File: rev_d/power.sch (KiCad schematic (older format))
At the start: 15 parts, among them J1 POWER_SELECT, Q1 PN2222, U1 LTV-826, U2 LTV-826, U3 LTV-826, U4 LTV-826, U5 LM2940, U6 754410

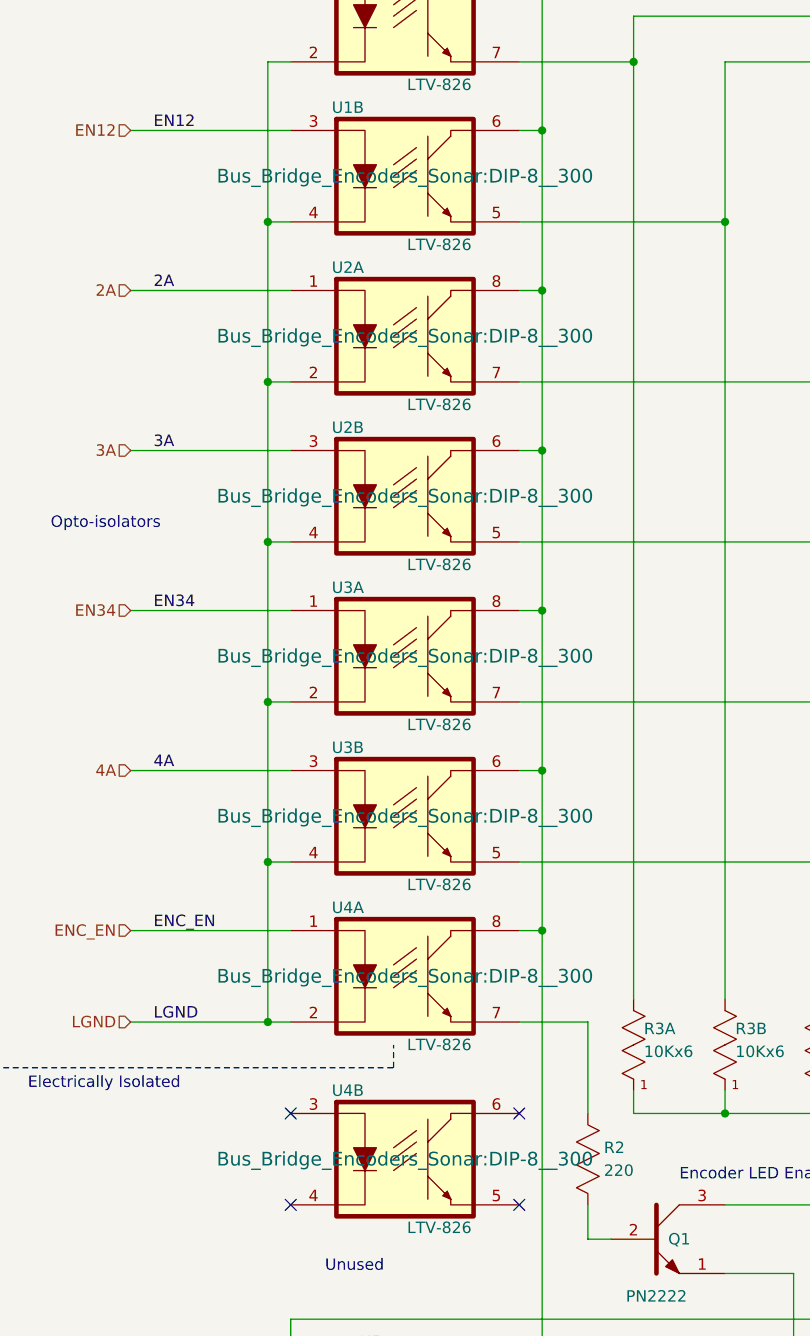
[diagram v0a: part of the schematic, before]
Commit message: Removed some ugliness from schematic.
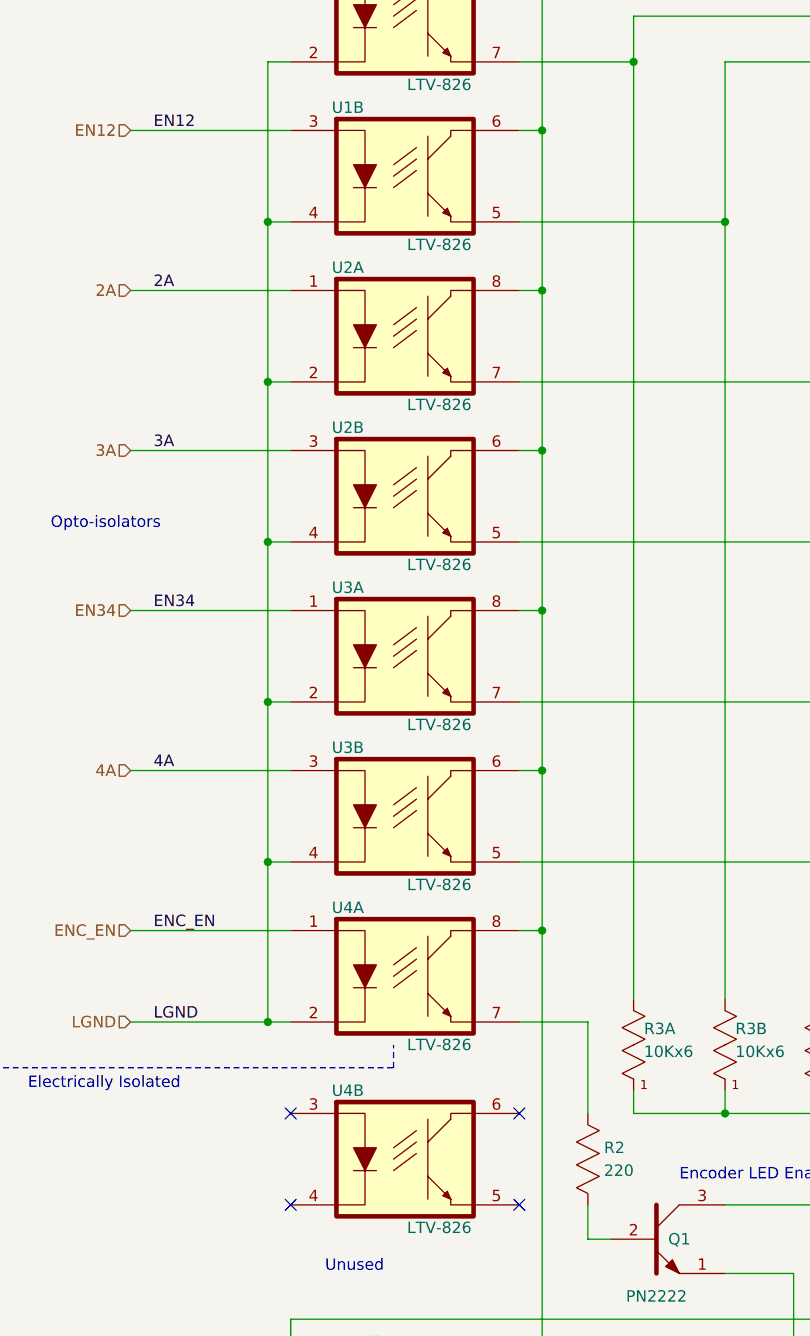
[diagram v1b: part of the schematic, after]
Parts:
- U1: footprint Bus_Bridge_Encoders_Sonar:DIP-8__300 -> (none)
- U2, U3, U4: footprint Bus_Bridge_Encoders_Sonar:DIP-8__300 -> ~
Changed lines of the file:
@@
 F 0 "U1" H 2050 1900 50  0000 C CNN
 F 1 "LTV-826" H 2450 1300 50  0000 C CNN
-F 2 "Bus_Bridge_Encoders_Sonar:DIP-8__300" H 2300 1600 60  0000 C CNN
+F 2 "" H 2300 1600 60  0000 C CNN
 F 3 "" H 2300 1600 60  0000 C CNN
 	2    2300 1600
@@
 F 0 "U2" H 2050 2600 50  0000 C CNN
 F 1 "LTV-826" H 2450 2000 50  0000 C CNN
-F 2 "Bus_Bridge_Encoders_Sonar:DIP-8__300" H 2300 2300 60  0000 C CNN
+F 2 "~" H 2300 2300 60  0000 C CNN
 F 3 "" H 2300 2300 60  0000 C CNN
 	1    2300 2300
@@
 F 0 "U2" H 2050 3300 50  0000 C CNN
 F 1 "LTV-826" H 2450 2700 50  0000 C CNN
-F 2 "Bus_Bridge_Encoders_Sonar:DIP-8__300" H 2300 3000 60  0000 C CNN
+F 2 "~" H 2300 3000 60  0000 C CNN
 F 3 "" H 2300 3000 60  0000 C CNN
 	2    2300 3000
@@
 F 0 "U3" H 2050 4000 50  0000 C CNN
 F 1 "LTV-826" H 2450 3400 50  0000 C CNN
-F 2 "Bus_Bridge_Encoders_Sonar:DIP-8__300" H 2300 3700 60  0000 C CNN
+F 2 "~" H 2300 3700 60  0000 C CNN
 F 3 "" H 2300 3700 60  0000 C CNN
 	1    2300 3700
@@
 F 0 "U3" H 2050 4700 50  0000 C CNN
 F 1 "LTV-826" H 2450 4100 50  0000 C CNN
-F 2 "Bus_Bridge_Encoders_Sonar:DIP-8__300" H 2300 4400 60  0000 C CNN
+F 2 "~" H 2300 4400 60  0000 C CNN
 F 3 "" H 2300 4400 60  0000 C CNN
 	2    2300 4400
@@
 F 0 "U4" H 2050 5400 50  0000 C CNN
 F 1 "LTV-826" H 2450 4800 50  0000 C CNN
-F 2 "Bus_Bridge_Encoders_Sonar:DIP-8__300" H 2300 5100 60  0000 C CNN
+F 2 "~" H 2300 5100 60  0000 C CNN
 F 3 "" H 2300 5100 60  0000 C CNN
 	1    2300 5100
@@
 F 0 "U4" H 2050 6200 50  0000 C CNN
 F 1 "LTV-826" H 2450 5600 50  0000 C CNN
-F 2 "Bus_Bridge_Encoders_Sonar:DIP-8__300" H 2300 5900 60  0000 C CNN
+F 2 "~" H 2300 5900 60  0000 C CNN
 F 3 "" H 2300 5900 60  0000 C CNN
 	2    2300 5900

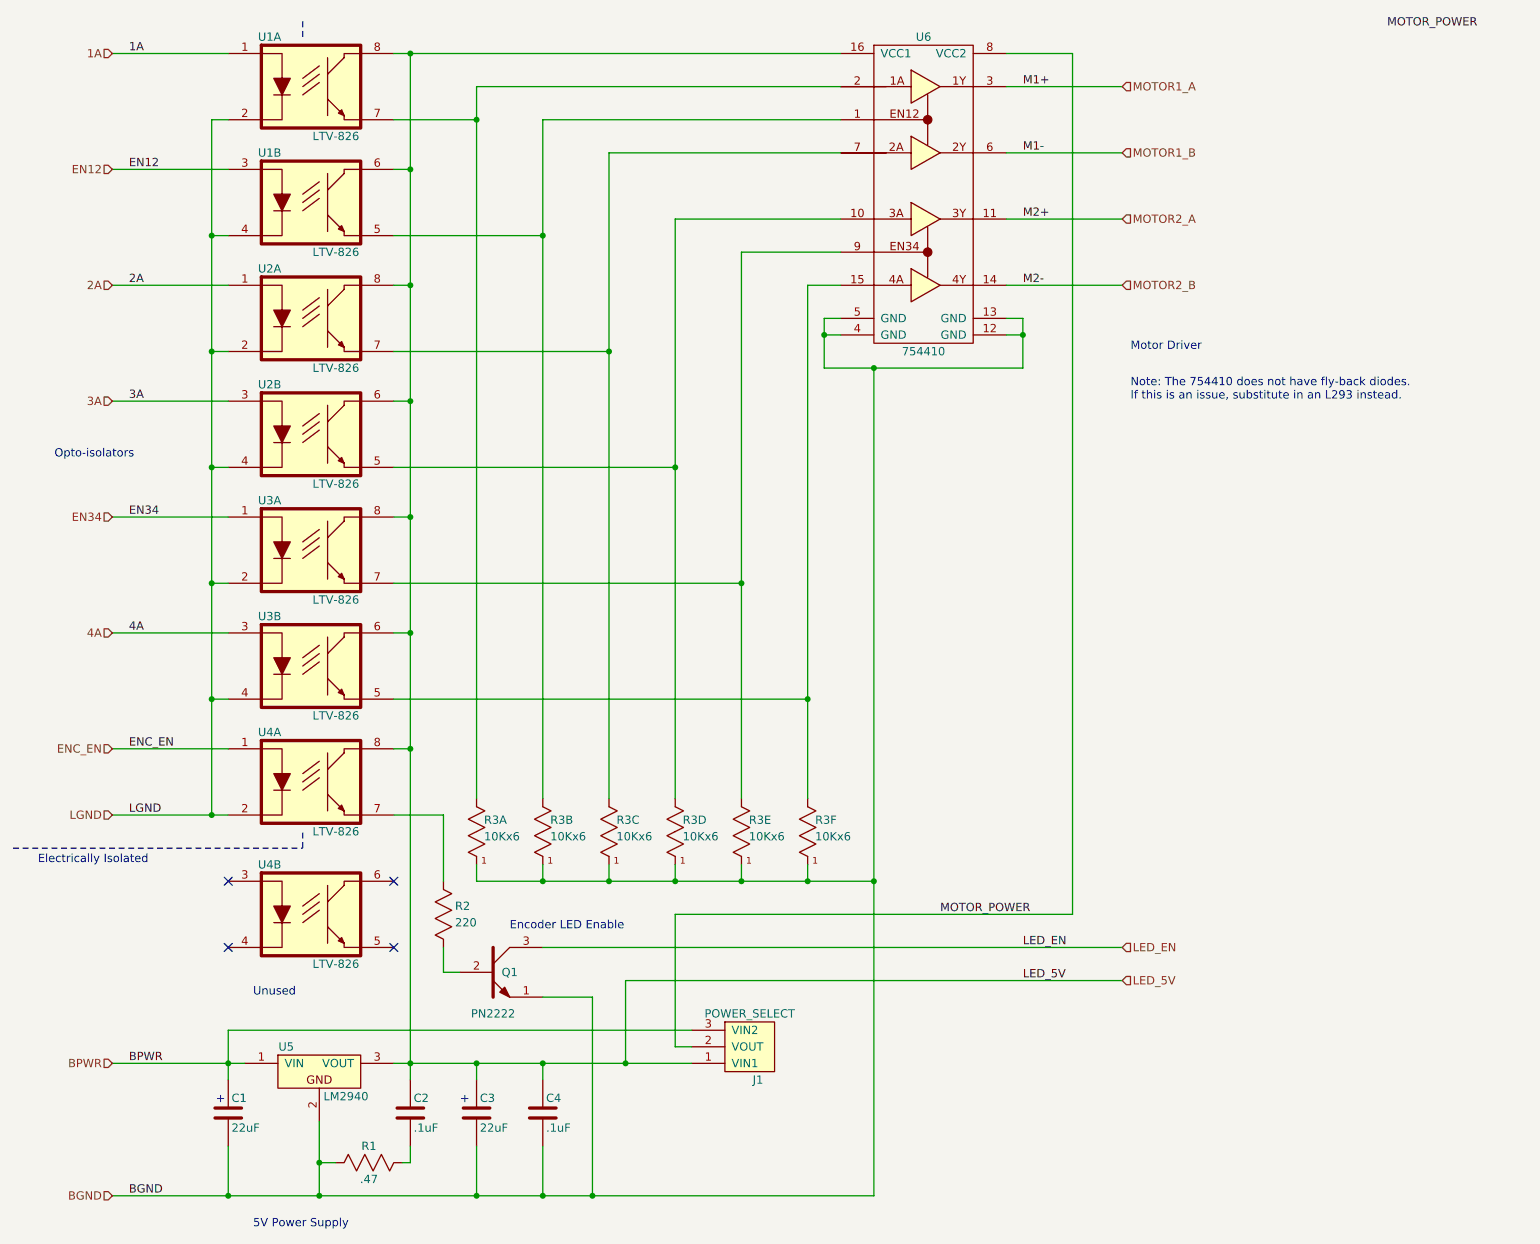
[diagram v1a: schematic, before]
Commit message: Split 22uF Capacitors into Aluminum and Tantalum.
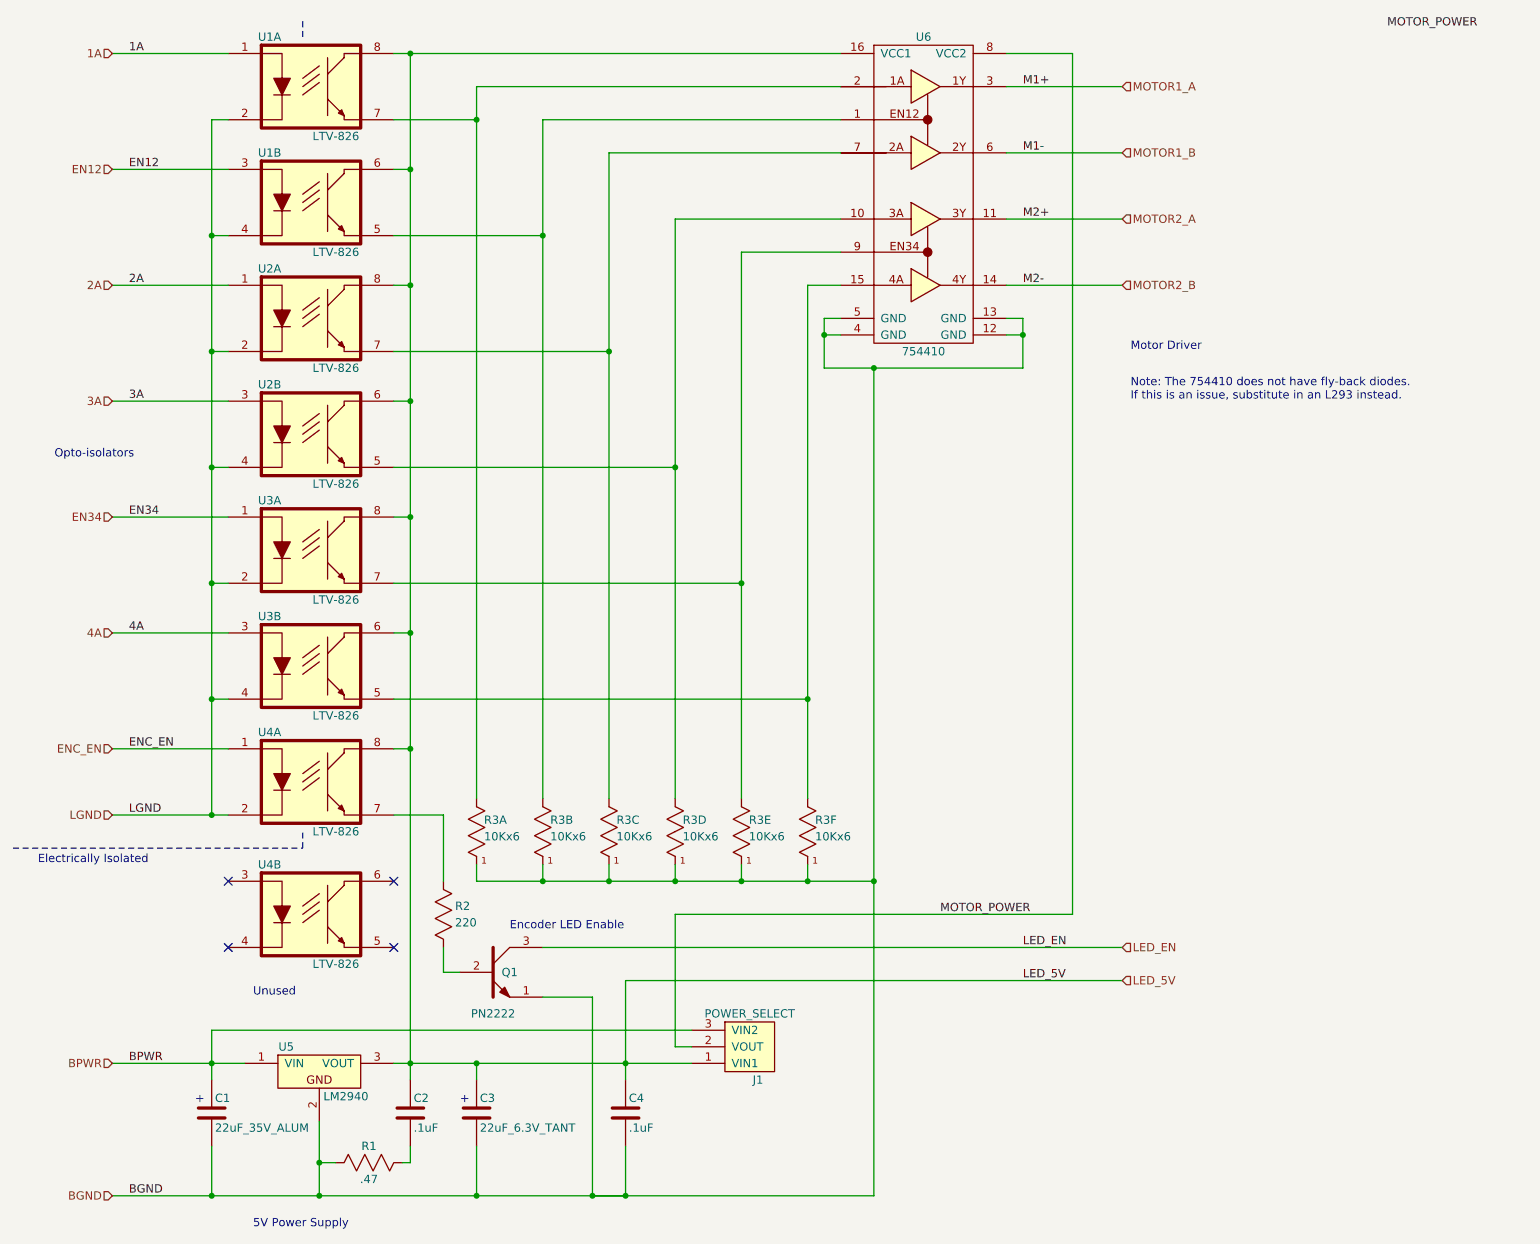
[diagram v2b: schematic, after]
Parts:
- C1: value 22uF -> 22uF_35V_ALUM
- C3: value 22uF -> 22uF_6.3V_TANT
- R1, R2: footprint Bus_Bridge_Encoders_Sonar:Pin_Header_Straight_1x02 -> Bus_Bridge_Encoders_Sonar:Resistor_Vertical__100
- U1: footprint (none) -> Bus_Bridge_Encoders_Sonar:DIP-8__300
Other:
- moved on the sheet: C1, C4
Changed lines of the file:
@@
 L C_VERT C1
 U 1 1 543A2450
-P 1800 7100
-F 0 "C1" H 1820 7190 50  0000 L CNN
-F 1 "22uF" H 1820 7010 50  0000 L CNN
-F 2 "Bus_Bridge_Encoders_Sonar:Capacitor3MMDiscRM2.5" H 1838 6950 30  0001 C CNN
-F 3 "" H 1800 7100 60  0000 C CNN
-	1    1800 7100
+P 1700 7100
+F 0 "C1" H 1720 7190 50  0000 L CNN
+F 1 "22uF_35V_ALUM" H 1720 7010 50  0000 L CNN
+F 2 "Bus_Bridge_Encoders_Sonar:Capacitor3MMDiscRM2.5" H 1738 6950 30  0001 C CNN
+F 3 "" H 1700 7100 60  0000 C CNN
+	1    1700 7100
 	1    0    0    -1
 $EndComp
@@
 F 0 "R1" H 2650 7500 50  0000 C CNN
 F 1 ".47" H 2650 7300 50  0000 C CNN
-F 2 "Bus_Bridge_Encoders_Sonar:Pin_Header_Straight_1x02" H 2675 7400 60  0001 C CNN
+F 2 "Bus_Bridge_Encoders_Sonar:Resistor_Vertical__100" H 2675 7400 60  0001 C CNN
 F 3 "" H 2675 7400 60  0000 C CNN
 	1    2650 7400
@@
 P 3300 7100
 F 0 "C3" H 3320 7190 50  0000 L CNN
-F 1 "22uF" H 3320 7010 50  0000 L CNN
+F 1 "22uF_6.3V_TANT" H 3320 7010 50  0000 L CNN
 F 2 "Bus_Bridge_Encoders_Sonar:Capacitor3MMDiscRM2.5" H 3338 6950 30  0001 C CNN
 F 3 "" H 3300 7100 60  0000 C CNN
@@
 L C_VERT C4
 U 1 1 543A249A
-P 3700 7100
-F 0 "C4" H 3720 7190 50  0000 L CNN
-F 1 ".1uF" H 3720 7010 50  0000 L CNN
-F 2 "Bus_Bridge_Encoders_Sonar:Capacitor4x3RM2-5_RevB" H 3738 6950 30  0001 C CNN
-F 3 "" H 3700 7100 60  0000 C CNN
-	1    3700 7100
+P 4200 7100
+F 0 "C4" H 4220 7190 50  0000 L CNN
+F 1 ".1uF" H 4220 7010 50  0000 L CNN
+F 2 "Bus_Bridge_Encoders_Sonar:Capacitor4x3RM2-5_RevB" H 4238 6950 30  0001 C CNN
+F 3 "" H 4200 7100 60  0000 C CNN
+	1    4200 7100
 	1    0    0    -1
 $EndComp
@@
 Text Label 6600 2100 0    50   ~ 0
 M2-
-Text Notes 1725 7050 0    50   ~ 0
+Text Notes 1600 7050 0    50   ~ 0
 +
 Text Notes 3200 7050 0    50   ~ 0
@@
 F 0 "U1" H 2050 1900 50  0000 C CNN
 F 1 "LTV-826" H 2450 1300 50  0000 C CNN
-F 2 "" H 2300 1600 60  0000 C CNN
+F 2 "Bus_Bridge_Encoders_Sonar:DIP-8__300" H 2300 1600 60  0001 C CNN
 F 3 "" H 2300 1600 60  0000 C CNN
 	2    2300 1600
@@
 F 0 "R2" H 3170 5950 50  0000 L CNN
 F 1 "220" H 3170 5850 50  0000 L CNN
-F 2 "Bus_Bridge_Encoders_Sonar:Pin_Header_Straight_1x02" H 3100 5950 60  0001 C CNN
+F 2 "Bus_Bridge_Encoders_Sonar:Resistor_Vertical__100" H 3100 5950 60  0001 C CNN
 F 3 "" H 3100 5950 60  0000 C CNN
 	1    3100 5900
@@
 Text HLabel 7200 6300 2    50   Input ~ 0
 LED_5V
-Connection ~ 1800 7600
+Connection ~ 1700 7600
 Connection ~ 2900 700
 Wire Wire Line
@@
 Connection ~ 1700 4600
 Wire Wire Line
-	1800 7600 1800 7300
+	1700 7600 1700 7300
 Connection ~ 1700 1800
 Wire Wire Line
@@
 	2850 7400 2900 7400
 Connection ~ 2350 7400
-Connection ~ 1800 6800
+Connection ~ 1700 6800
 Wire Wire Line
 	1100 6800 1900 6800
@@
 	5500 1300 4100 1300
 Wire Wire Line
-	5700 7600 5700 2600
+	5700 2600 5700 7600
 Connection ~ 5700 2600
 Wire Wire Line
 	5400 2600 6600 2600
 Wire Wire Line
-	1100 7600 5700 7600
+	1100 7600 4200 7600
+Wire Wire Line
+	5700 7600 4000 7600
 Wire Wire Line
 	2350 7150 2350 7600
@@
 	3300 6800 3300 6900
 Wire Wire Line
-	1800 6600 1800 6900
+	1700 6600 1700 6900
 Connection ~ 3300 7600
 Connection ~ 2900 4900
 Wire Wire Line
-	3700 6800 3700 6900
-Wire Wire Line
-	3700 7300 3700 7600
-Connection ~ 3700 7600
+	4200 7600 4200 7300
+Connection ~ 4200 7600
 Wire Wire Line
 	3300 5700 5700 5700
 Connection ~ 5700 5700
-Connection ~ 3700 6800
-Wire Wire Line
-	4600 6600 1800 6600
+Wire Wire Line
+	4600 6600 1700 6600
 Wire Wire Line
 	4600 6700 4500 6700
@@
 	7200 6300 4200 6300
 Wire Wire Line
-	4200 6300 4200 6800
+	4200 6300 4200 6900
 Connection ~ 4200 6800
 Wire Wire Line
